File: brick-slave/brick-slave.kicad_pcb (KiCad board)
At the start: 2 copper layers, 52.3 x 72.4 mm, 4 parts, among them J1 Conn_01x06_Male, J2 Conn_01x06_Male, J3 Conn_01x06_Female, J4 Conn_01x06_Female

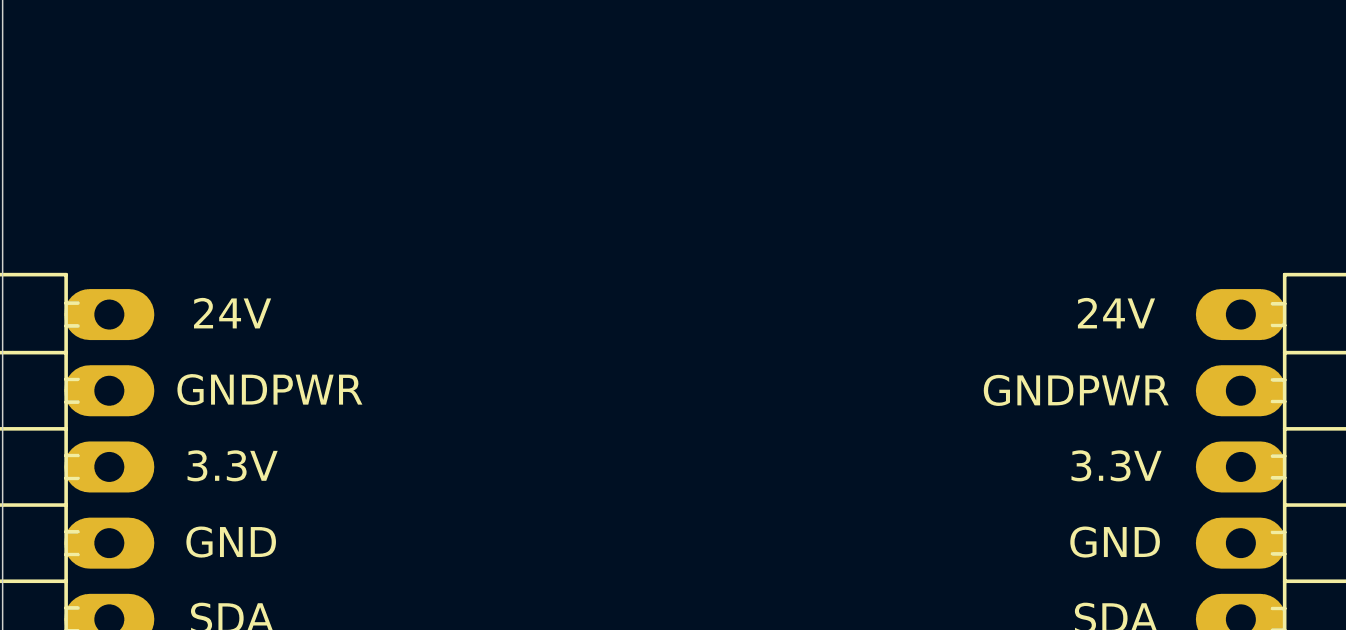
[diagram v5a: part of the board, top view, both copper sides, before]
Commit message: change PWR voltage
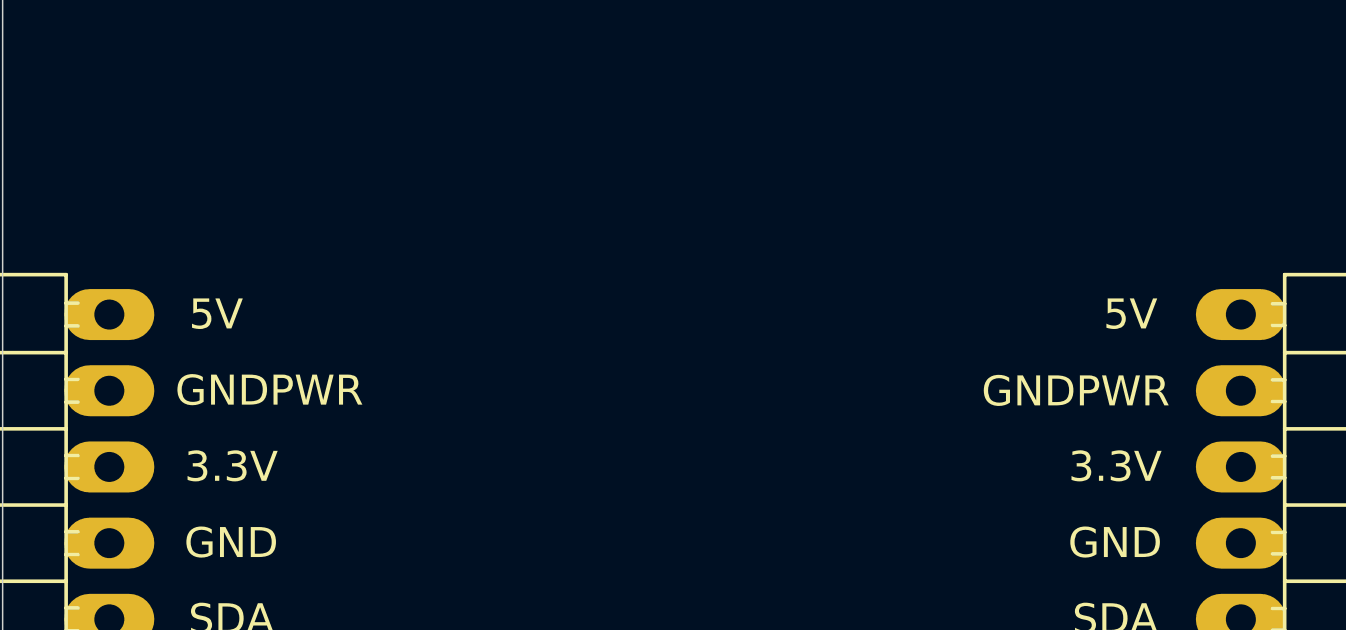
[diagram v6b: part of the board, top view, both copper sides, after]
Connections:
- net +24V renamed +5V
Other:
- board text added: "5V"
- board text removed: "24V"
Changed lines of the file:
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@@
   )
   (net 0 "")
-  (net 1 "+24V")
+  (net 1 "+5V")
   (net 2 "GNDPWR")
   (net 3 "+3V3")
@@
     (descr "Through hole angled socket strip, 1x06, 2.54mm pitch, 8.51mm socket length, single row (from Kicad 4.0.7), script generated")
     (tags "Through hole angled socket strip THT 1x06 2.54mm single row")
+    (property "Sheetfile" "brick-slave.kicad_sch")
+    (property "Sheetname" "")
     (attr through_hole)
     (fp_text reference "J4" (at -4.38 -2.77) (layer "F.SilkS")
@@
     (fp_line (start -10.03 13.97) (end -10.03 -1.27) (layer "F.Fab") (width 0.1))
     (pad "1" thru_hole rect locked (at 0 0 180) (size 3 1.7) (drill 1) (layers *.Cu *.Mask)
-      (net 9 "GPIO4"))
+      (net 9 "GPIO4") (pinfunction "Pin_1"))
     (pad "2" thru_hole oval locked (at 0 2.54 180) (size 3 1.7) (drill 1) (layers *.Cu *.Mask)
-      (net 8 "GPIO5"))
+      (net 8 "GPIO5") (pinfunction "Pin_2"))
     (pad "3" thru_hole oval locked (at 0 5.08 180) (size 3 1.7) (drill 1) (layers *.Cu *.Mask)
-      (net 12 "GPIO14"))
+      (net 12 "GPIO14") (pinfunction "Pin_3"))
     (pad "4" thru_hole oval locked (at 0 7.62 180) (size 3 1.7) (drill 1) (layers *.Cu *.Mask)
-      (net 7 "GPIO15"))
+      (net 7 "GPIO15") (pinfunction "Pin_4"))
     (pad "5" thru_hole oval locked (at 0 10.16 180) (size 3 1.7) (drill 1) (layers *.Cu *.Mask)
-      (net 11 "GPIO35"))
+      (net 11 "GPIO35") (pinfunction "Pin_5"))
     (pad "6" thru_hole oval locked (at 0 12.7 180) (size 3 1.7) (drill 1) (layers *.Cu *.Mask)
-      (net 10 "GPIO36"))
+      (net 10 "GPIO36") (pinfunction "Pin_6"))
     (model "${KISYS3DMOD}/Connector_PinSocket_2.54mm.3dshapes/PinSocket_1x06_P2.54mm_Horizontal.wrl"
       (offset (xyz 0 0 0))
@@
     (descr "Through hole angled pin header, 1x06, 2.54mm pitch, 6mm pin length, single row")
     (tags "Through hole angled pin header THT 1x06 2.54mm single row")
+    (property "Sheetfile" "brick-slave.kicad_sch")
+    (property "Sheetname" "")
     (attr through_hole)
     (fp_text reference "J1" (at 1.27 -2.54) (layer "F.SilkS")
@@
     (fp_line (start -0.32 4.76) (end 1.5 4.76) (layer "F.Fab") (width 0.1))
     (pad "1" thru_hole rect locked (at 0 0 180) (size 3 1.7) (drill 1) (layers *.Cu *.Mask)
-      (net 5 "SCL"))
+      (net 5 "SCL") (pinfunction "Pin_1"))
     (pad "2" thru_hole oval locked (at 0 2.54 180) (size 3 1.7) (drill 1) (layers *.Cu *.Mask)
-      (net 6 "SDA"))
+      (net 6 "SDA") (pinfunction "Pin_2"))
     (pad "3" thru_hole oval locked (at 0 5.08 180) (size 3 1.7) (drill 1) (layers *.Cu *.Mask)
-      (net 4 "GND"))
+      (net 4 "GND") (pinfunction "Pin_3"))
     (pad "4" thru_hole oval locked (at 0 7.62 180) (size 3 1.7) (drill 1) (layers *.Cu *.Mask)
-      (net 3 "+3V3"))
+      (net 3 "+3V3") (pinfunction "Pin_4"))
     (pad "5" thru_hole oval locked (at 0 10.16 180) (size 3 1.7) (drill 1) (layers *.Cu *.Mask)
-      (net 2 "GNDPWR"))
+      (net 2 "GNDPWR") (pinfunction "Pin_5"))
     (pad "6" thru_hole oval locked (at 0 12.7 180) (size 3 1.7) (drill 1) (layers *.Cu *.Mask)
-      (net 1 "+24V"))
+      (net 1 "+5V") (pinfunction "Pin_6"))
     (model "${KISYS3DMOD}/Connector_PinHeader_2.54mm.3dshapes/PinHeader_1x06_P2.54mm_Horizontal.wrl"
       (offset (xyz 0 0 0))
@@
     (descr "Through hole angled pin header, 1x06, 2.54mm pitch, 6mm pin length, single row")
     (tags "Through hole angled pin header THT 1x06 2.54mm single row")
+    (property "Sheetfile" "brick-slave.kicad_sch")
+    (property "Sheetname" "")
     (attr through_hole)
     (fp_text reference "J2" (at 1.27 -2.54) (layer "F.SilkS")
@@
     (fp_line (start -0.32 7.94) (end 1.5 7.94) (layer "F.Fab") (width 0.1))
     (pad "1" thru_hole rect locked (at 0 0 180) (size 3 1.7) (drill 1) (layers *.Cu *.Mask)
-      (net 9 "GPIO4"))
+      (net 9 "GPIO4") (pinfunction "Pin_1"))
     (pad "2" thru_hole oval locked (at 0 2.54 180) (size 3 1.7) (drill 1) (layers *.Cu *.Mask)
-      (net 8 "GPIO5"))
+      (net 8 "GPIO5") (pinfunction "Pin_2"))
     (pad "3" thru_hole oval locked (at 0 5.08 180) (size 3 1.7) (drill 1) (layers *.Cu *.Mask)
-      (net 12 "GPIO14"))
+      (net 12 "GPIO14") (pinfunction "Pin_3"))
     (pad "4" thru_hole oval locked (at 0 7.62 180) (size 3 1.7) (drill 1) (layers *.Cu *.Mask)
-      (net 7 "GPIO15"))
+      (net 7 "GPIO15") (pinfunction "Pin_4"))
     (pad "5" thru_hole oval locked (at 0 10.16 180) (size 3 1.7) (drill 1) (layers *.Cu *.Mask)
-      (net 11 "GPIO35"))
+      (net 11 "GPIO35") (pinfunction "Pin_5"))
     (pad "6" thru_hole oval locked (at 0 12.7 180) (size 3 1.7) (drill 1) (layers *.Cu *.Mask)
-      (net 10 "GPIO36"))
+      (net 10 "GPIO36") (pinfunction "Pin_6"))
     (model "${KISYS3DMOD}/Connector_PinHeader_2.54mm.3dshapes/PinHeader_1x06_P2.54mm_Horizontal.wrl"
       (offset (xyz 0 0 0))
@@
     (descr "Through hole angled socket strip, 1x06, 2.54mm pitch, 8.51mm socket length, single row (from Kicad 4.0.7), script generated")
     (tags "Through hole angled socket strip THT 1x06 2.54mm single row")
+    (property "Sheetfile" "brick-slave.kicad_sch")
+    (property "Sheetname" "")
     (attr through_hole)
     (fp_text reference "J3" (at -4.38 -2.77) (layer "F.SilkS")
@@
     (fp_line (start -1.52 2.84) (end 0 2.84) (layer "F.Fab") (width 0.1))
     (pad "1" thru_hole rect locked (at 0 0 180) (size 3 1.7) (drill 1) (layers *.Cu *.Mask)
-      (net 5 "SCL"))
+      (net 5 "SCL") (pinfunction "Pin_1"))
     (pad "2" thru_hole oval locked (at 0 2.54 180) (size 3 1.7) (drill 1) (layers *.Cu *.Mask)
-      (net 6 "SDA"))
+      (net 6 "SDA") (pinfunction "Pin_2"))
     (pad "3" thru_hole oval locked (at 0 5.08 180) (size 3 1.7) (drill 1) (layers *.Cu *.Mask)
-      (net 4 "GND"))
+      (net 4 "GND") (pinfunction "Pin_3"))
     (pad "4" thru_hole oval locked (at 0 7.62 180) (size 3 1.7) (drill 1) (layers *.Cu *.Mask)
-      (net 3 "+3V3"))
+      (net 3 "+3V3") (pinfunction "Pin_4"))
     (pad "5" thru_hole oval locked (at 0 10.16 180) (size 3 1.7) (drill 1) (layers *.Cu *.Mask)
-      (net 2 "GNDPWR"))
+      (net 2 "GNDPWR") (pinfunction "Pin_5"))
     (pad "6" thru_hole oval locked (at 0 12.7 180) (size 3 1.7) (drill 1) (layers *.Cu *.Mask)
-      (net 1 "+24V"))
+      (net 1 "+5V") (pinfunction "Pin_6"))
     (model "${KISYS3DMOD}/Connector_PinSocket_2.54mm.3dshapes/PinSocket_1x06_P2.54mm_Horizontal.wrl"
       (offset (xyz 0 0 0))
@@
   (gr_arc (start 113.284 124.46) (end 113.284 127) (angle -90) (layer "Edge.Cuts") (width 0.05))
   (gr_arc (start 113.284 57.15) (end 115.824 57.15) (angle -90) (layer "Edge.Cuts") (width 0.05))
-  (gr_text "24V" (at 100.584 86.36) (layer "F.SilkS")
+  (gr_text "5V" (at 101.092 86.36) (layer "F.SilkS")
     (effects (font (size 1 1) (thickness 0.15)))
   )
@@
     (effects (font (size 1 1) (thickness 0.15)))
   )
-  (gr_text "24V" (at 71.12 86.36) (layer "F.SilkS")
-    (effects (font (size 1 1) (thickness 0.15)))
-  )
+  (gr_text "5V" (at 70.612 86.36) (layer "F.SilkS")
+    (effects (font (size 1 1) (thickness 0.15)))
+  )

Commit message: refactor brick-slave
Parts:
- added H1: MountingHole, MountingHole:MountingHole_3.2mm_M3, F.Cu at (67.1, 58.9)
- added H2: MountingHole, MountingHole:MountingHole_3.2mm_M3, F.Cu at (129.5, 58.9)
- added H3: MountingHole, MountingHole:MountingHole_3.2mm_M3, F.Cu at (67.1, 123.4)
- added H4: MountingHole, MountingHole:MountingHole_3.2mm_M3, F.Cu at (129.5, 123.4)
- moved J4 18.0 mm to (122.1, 116.9)
- moved J3 17.5 mm to (122.1, 96.5)
- moved J2 5.05 mm to (67.1, 116.9)
- moved J1 2.56 mm to (67.1, 96.5)
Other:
- board size 52.3 x 72.4 mm -> 69.6 x 71.6 mm
